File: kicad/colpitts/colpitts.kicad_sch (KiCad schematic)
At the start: 12 parts, among them Q1 2N2222

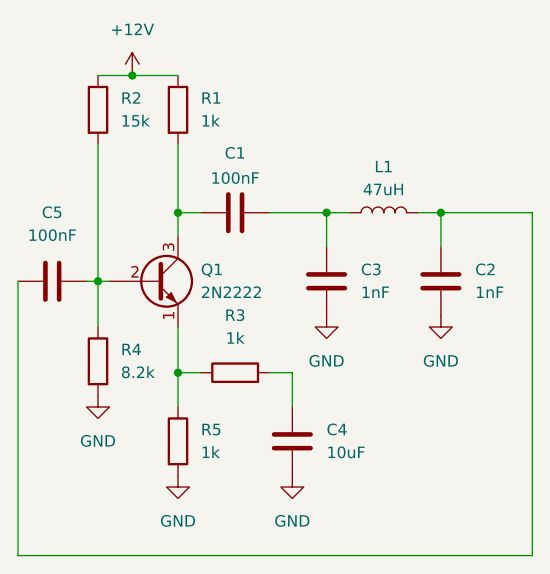
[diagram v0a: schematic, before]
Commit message: update schem, clean up ising sim
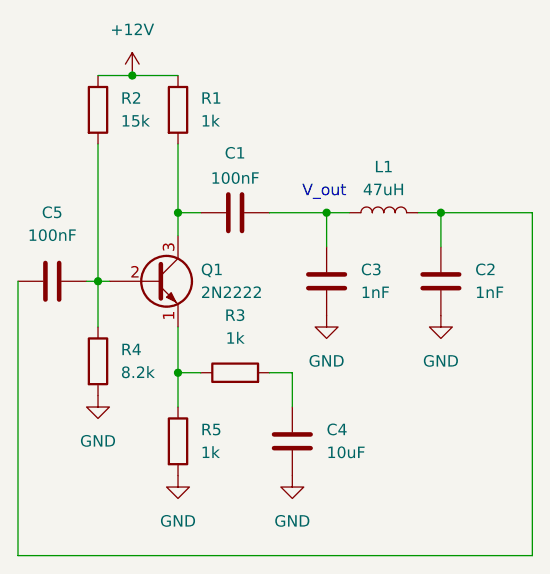
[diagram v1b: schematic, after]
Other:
- note added: "V_out"
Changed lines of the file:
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@@
+		)
+	)
+	(text "V_out"
+		(exclude_from_sim no)
+		(at 169.926 91.694 0)
+		(effects
+			(font
+				(size 1.27 1.27)
+			)
 		)
 	)
